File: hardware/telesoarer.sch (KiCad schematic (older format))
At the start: 30 parts, among them IC1 ATMEGA328P, K1 RC SIG IN, K2 G T R, P1 ATMEL ISP, P2 PZ, P3 PZ_IN, P4 AOUT, Q1 BC847C, Q2 2N7000, U1 MS5611

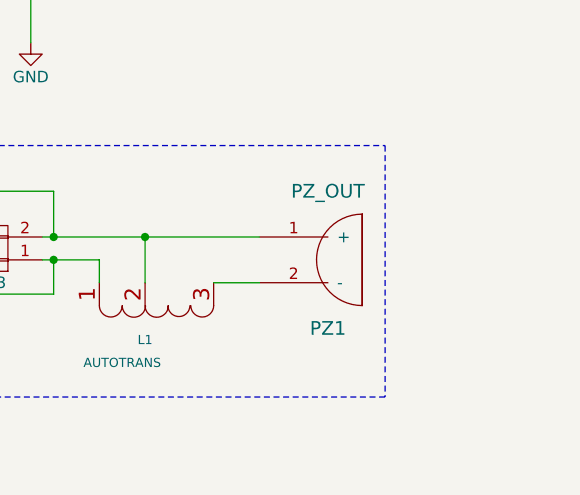
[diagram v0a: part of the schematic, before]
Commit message: Moved high voltage piezo output away from delicate analog output. Other minor changes.
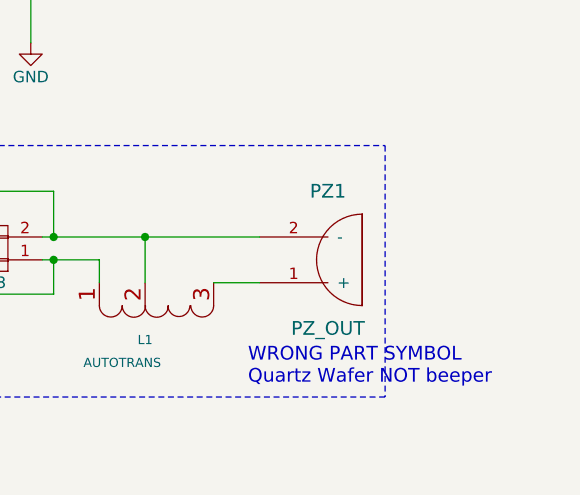
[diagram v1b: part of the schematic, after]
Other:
- note added: "WRONG PART SYMBOL\nQuartz Wafer NOT beeper"
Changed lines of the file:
@@
 F 3 "" H 9500 5450 60  0001 C CNN
 	1    9500 5450
-	1    0    0    -1
+	1    0    0    1
 $EndComp
 $Comp
@@
 Connection ~ 8400 5450
 Connection ~ 7200 5600
+Text Notes 9250 6000 0    60   ~ 0
+WRONG PART SYMBOL\nQuartz Wafer NOT beeper
 $EndSCHEMATC

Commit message: Need 16MHz xtal for Arduino bootloader serial to work -- clock too inaccurate at 8MHz RC. Added OLED display and the somewhat important 3.3V regulator I completely forgot about before!
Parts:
- removed K2: G T R, footprints:TP-3, symbol CONN_01X03
- added C10, C11, C12, C13: 1u, footprints:C_0603, symbol C-RESCUE-telesoarer-mlf
- added C14, C15: 2u2, footprints:C_0603, symbol C-RESCUE-telesoarer-mlf
- added C5, C6: 18p, footprints:C_0603, symbol C-RESCUE-telesoarer-mlf
- added C7, C9: 0u1, footprints:C_0603, symbol C-RESCUE-telesoarer-mlf
- added C8: 22u, footprints:TantalC_SizeS_EIA-3216, symbol CP
- added P5: OLED 0.91\" 128x32, symbol CONN_01X15
- added R12: 1K, footprints:R_0603, symbol R
- added R13: 0, footprints:R_0603, symbol R
- added R14: 390K, footprints:R_0603, symbol R
- added U2: LM1117IMP-3.3/NOPB, TO_SOT_Packages_SMD:SOT-223, symbol AP111733
- added X1: 16MHz, symbol CRYSTAL_SMD
- K1: value RC SIG IN -> DATA; symbol CONN_01X03 -> CONN_01X06
- R1: value 5K6 -> 10K
- R2: value 200 -> 1K
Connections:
- net labels added: +BATT, D/~C, OLED_~SS, RX, SENS_~SS, TX, VBAT, VDD, VSS, ~RES, ~RESET
- net labels removed: +5V, RESET, ~SS
- wire segments 96 -> 147
- no-connect marks 13 -> 8
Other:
- note added: "All ATmega328 I/O pins have clamping diodes and \ntherefore should be fine sinking 5V, so long as a \nseries current limiting resistor is present."
- note added: "MCU 5 Volt SIG & RX inputs with 3.3V VDD"
- note added: "WRONG SYMBOL\nQuartz Wafer\nNOT beeper"
- note removed: "Debug UART\nBreak-out"
- note removed: "WRONG PART SYMBOL\nQuartz Wafer NOT beeper"
- moved on the sheet: C1, C2, C3, C4, D1, D2, D3, P4, Q2, R1, R10, R11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

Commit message: Switching to NXP ARM chip. Added reference files.
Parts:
- removed C2: 22u, footprints:TantalC_SizeS_EIA-3216, symbol CP
- removed U2: LM1117IMP-3.3/NOPB, TO_SOT_Packages_SMD:SOT-223, symbol AP111733
- added U2: MCP1703T-3302, footprints:SOT-23A, symbol MCP1703T-3302
- C1: renamed from C4; footprint footprints:C_0603 -> footprints:C_0402
- C10: renamed from C11; footprint footprints:C_0603 -> footprints:C_0402
- C11: renamed from C12; footprint footprints:C_0603 -> footprints:C_0402
- C12: renamed from C13; footprint footprints:C_0603 -> footprints:C_0402
- C13: renamed from C14; footprint footprints:C_0603 -> footprints:C_0402
- C14: renamed from C15; footprint footprints:C_0603 -> footprints:C_0402
- C2: renamed from C7; footprint footprints:C_0603 -> footprints:C_0402
- C4: renamed from C5; footprint footprints:C_0603 -> footprints:C_0402
- C5: renamed from C9; footprint footprints:C_0603 -> footprints:C_0402
- C6: footprint footprints:C_0603 -> footprints:C_0402
- C7: renamed from C1; footprint footprints:C_0603 -> footprints:C_0402
- C8: renamed from C3; footprint footprints:C_0603 -> footprints:C_0402
- C9: renamed from C10; footprint footprints:C_0603 -> footprints:C_0402
- K1: footprint footprints:SIL-3 -> Pin_Headers:Pin_Header_Angled_1x06
- P5: footprint (none) -> footprints:ZIF_FPC15
- R1, R14, R2, R3, R4, R5: footprint footprints:R_0603 -> footprints:R_0402
- R10: renamed from R8; footprint footprints:R_0603 -> footprints:R_0402
- R11: renamed from R9; footprint footprints:R_0603 -> footprints:R_0402
- R12: renamed from R10; footprint footprints:R_0603 -> footprints:R_0402
- R13: renamed from R11; footprint footprints:R_0603 -> footprints:R_0402
- R6: renamed from R12; footprint footprints:R_0603 -> footprints:R_0402
- R7: renamed from R13; footprint footprints:R_0603 -> footprints:R_0402
- R8: renamed from R7; footprint footprints:R_0603 -> footprints:R_0402
- R9: renamed from R6; footprint footprints:R_0603 -> footprints:R_0402
- X1: footprint (none) -> Crystals:Crystal_SMD_2520_4Pads
- renumbered C8 to C3
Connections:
- wire segments 147 -> 139
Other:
- moved on the sheet: C1, C7

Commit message: Ripping things apart for the change to STM32 chipa
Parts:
- removed C2: 0u1, footprints:C_0402, symbol C-RESCUE-telesoarer-mlf
- removed IC1: ATMEGA328P, footprints:MLF-32_2mmVIA_SINK, symbol ATMEGA328P
- removed P1: ATMEL ISP, footprints:PIN_ARRAY_3x2_GRUVIN, symbol CONN_01X06
- removed R1: 10K, footprints:R_0402, symbol R
- removed R6: 1K, footprints:R_0402, symbol R
- removed R7: 0, footprints:R_0402, symbol R
- added C7, C8, C9: 0u1, footprints:C_0402, symbol C-RESCUE-telesoarer-mlf
- added IC1: STM32F103TBU6, footprints:VFQFPN36_0.5_6x6, symbol STM32F103TBU6
- added K2: SERIAL, Pin_Headers:Pin_Header_Angled_1x03, symbol CONN_01X03
- added K3: DEBUG, Pin_Headers:Pin_Header_Angled_1x03, symbol CONN_01X03
- added R2: NC, footprints:R_0603, symbol R
- added R3: 5K, footprints:R_0402, symbol R
- K1: value DATA -> RC_SIG; footprint Pin_Headers:Pin_Header_Angled_1x06 -> Pin_Headers:Pin_Header_Angled_1x03; symbol CONN_01X06 -> CONN_01X03
- renumbered C8 to C10, C9 to C11, C10 to C12, C11 to C13, C12 to C14, C13 to C15, C14 to C16, C4 to C2, C6 to C4, C7 to C6, P2 to P1, P3 to P2, P4 to P3, P5 to P4, R2 to R1, R11 to R10, R12 to R11, R13 to R12, R14 to R13, R3 to R4, R4 to R5, R5 to R6, R9 to R7, R10 to R9
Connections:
- net labels added: OLED_D/~C, OLED_~RES, SWDCLK, SWDIO, USART1_RX, USART1_TX, USRAT1_RX
- net labels removed: D/~C, RX, TX, ~RES
- wire segments 139 -> 152
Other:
- note removed: "3x2 pogo\npin pads"
- moved on the sheet: C1, C10, C13, C14, C2, C3, C4, C5, C6, D1, D2, D3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

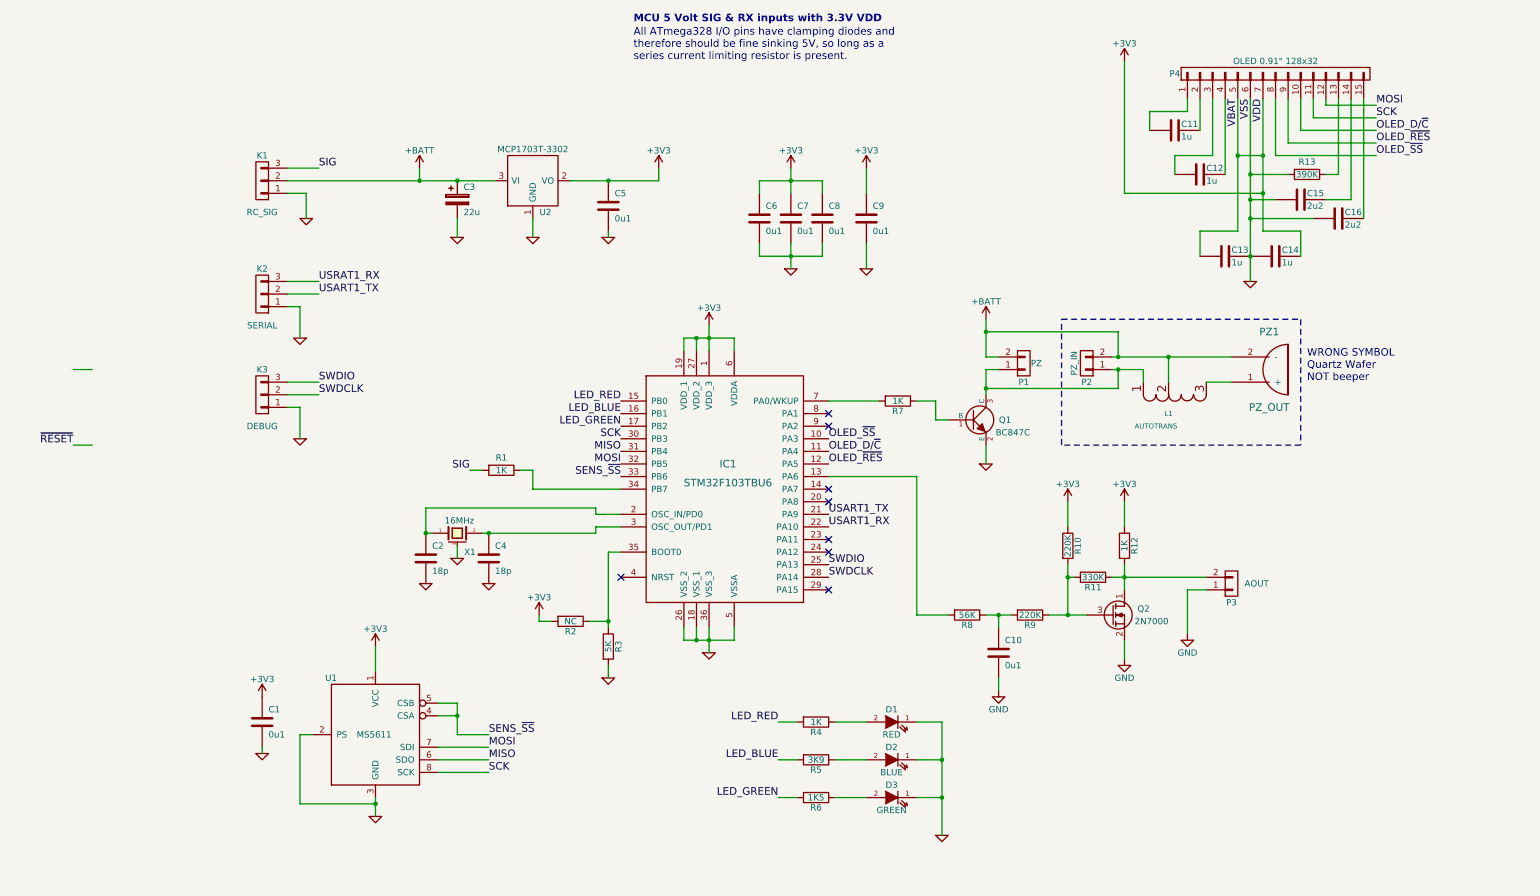
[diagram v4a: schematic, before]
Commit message: Schematic updates for change to STM32F103 MCU
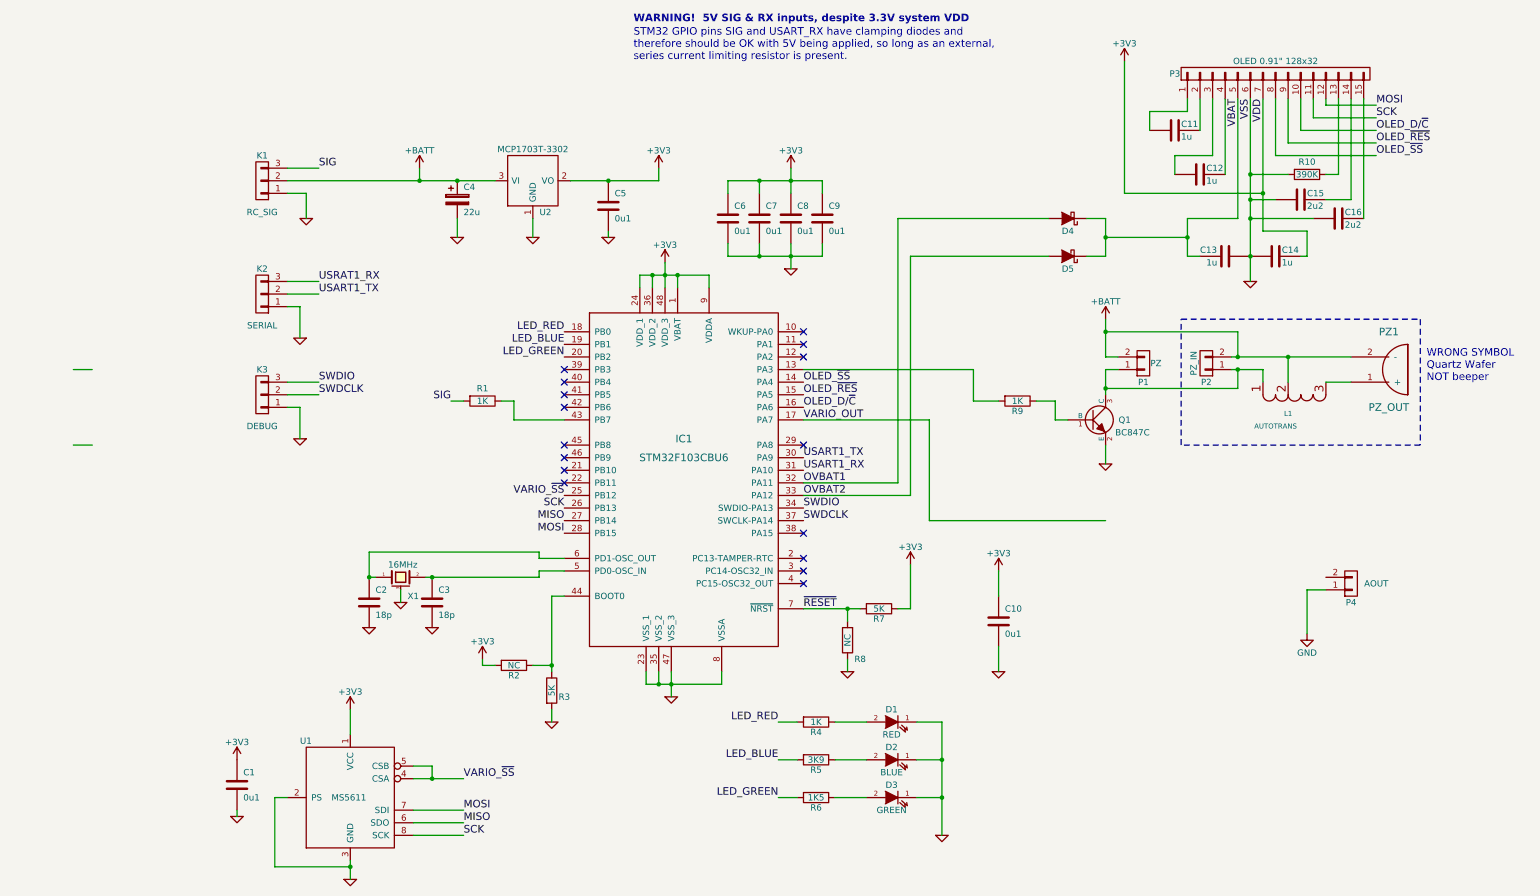
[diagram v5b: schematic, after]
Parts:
- removed C10: 0u1, footprints:C_0402, symbol C-RESCUE-telesoarer-mlf
- removed IC1: STM32F103TBU6, footprints:VFQFPN36_0.5_6x6, symbol STM32F103TBU6
- removed Q2: 2N7000, TO_SOT_Packages_SMD:SOT-23, symbol Q_NMOS_DSG
- removed R10, R9: 220K, footprints:R_0402, symbol R
- removed R11: 330K, footprints:R_0402, symbol R
- removed R12: 1K, footprints:R_0402, symbol R
- added C6: 0u1, footprints:C_0402, symbol C-RESCUE-telesoarer-mlf
- added D4, D5: D_Schottky, symbol D_Schottky
- added IC1: STM32F103CBU6, symbol STM32F103CBU6
- added R7: 5K, footprints:R_0402, symbol R
- R8: value 56K -> NC
- renumbered C9 to C10, C4 to C3, C3 to C4, C6 to C7, C7 to C8, C8 to C9, P4 to P3, P3 to P4, R13 to R10, R7 to R9
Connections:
- net +3V3: now also C6.1, IC1.1 (VBAT), IC1.24 (VDD_1), IC1.36 (VDD_2), IC1.48 (VDD_3), IC1.9 (VDDA), R7.1; no longer C13.2, P3.5 (P5)
- net GND: now also R8.1, C6.2, IC1.23 (VSS_1), IC1.35 (VSS_2), IC1.47 (VSS_3), IC1.8 (VSSA)
- net LED_BLUE: now also IC1.19 (PB1)
- net LED_GREEN: now also IC1.20 (PB2)
- net LED_RED: now also IC1.18 (PB0)
- net MISO: now also IC1.27 (PB14)
- net MOSI: now also IC1.28 (PB15)
- net OLED_D/~C: now also IC1.16 (PA6)
- net OLED_~RES: now also IC1.15 (PA5)
- net OLED_~SS: now also IC1.14 (PA4)
- net SCK: now also IC1.26 (PB13)
- net SWDCLK: now also IC1.37 (SWCLK-PA14)
- net SWDIO: now also IC1.34 (SWDIO-PA13)
- net USART1_RX: now also IC1.31 (PA10)
- net USART1_TX: now also IC1.30 (PA9)
- net ~RESET: now also R8.2, IC1.7 (~NRST), R7.2
- net at R9.2: now also IC1.13 (PA3)
- net at R1.1: now also IC1.43 (PB7)
- net at C2.1, X1.1: now also IC1.6 (PD1-OSC_OUT)
- net at C3.1, X1.2: now also IC1.5 (PD0-OSC_IN)
- net at R2.1, R3.1: now also IC1.44 (BOOT0)
- net SENS_~SS renamed VARIO_~SS
- net VARIO_~SS: now also IC1.25 (PB12)
- new net OVBAT1: D4.2 (A), IC1.32 (PA11)
- new net OVBAT2: D5.2 (A), IC1.33 (PA12)
- new net VARIO_OUT: IC1.17 (PA7)
- new net VBAT: C13.2, D4.1 (K), D5.1 (K), P3.5 (P5)
- no-connect marks 8 -> 16
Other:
- note added: "STM32 GPIO pins SIG and USART_RX have clamping diodes and \ntherefore should be OK with 5V being applied, so long as an external,\nseries current limiting resistor is present."
- note added: "WARNING! 5V SIG & RX inputs, despite 3.3V system VDD"
- note removed: "All ATmega328 I/O pins have clamping diodes and \ntherefore should be fine sinking 5V, so long as a \nseries current limiting resistor is present."
- note removed: "MCU 5 Volt SIG & RX inputs with 3.3V VDD"
- moved on the sheet: C1, C10, C2, C3, L1, P1, P2, P4, PZ1, Q1, R1, R2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

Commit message: Completed first draft of STM32 based schematic. (Added Vario output LPF.)
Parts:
- added C11, C14: 0u1, footprints:C_0402, symbol C-RESCUE-telesoarer-mlf
- added R10, R11: 5K, footprints:R_0402, symbol R
- added R12, R15: 100K, footprints:R_0402, symbol R
- added R13: 100, footprints:R_0402, symbol R
- added U3: AD8027ARTZ, symbol AD8027ARTZ
- C2, C3: symbol C-RESCUE-telesoarer-mlf -> C
- renumbered C11 to C12, C12 to C13, C13 to C15, C14 to C16, C15 to C17, C16 to C18, R10 to R14, R8 to R7, R7 to R8
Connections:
- net USRAT1_RX is gone; now on net USART1_RX: K2.3 (P3)
- net +3V3: now also U3.6 (V+)
- net GND: now also C11.2, C14.2, R13.1, U3.2 (V-)
- net VARIO_OUT: now also R10.2
- net at P4.2 (P2): now also R15.2, U3.1
- new net: R12.2, U3.3 (+)
- new net: R13.2, R15.1, U3.4 (-)
- new net: C14.1, R11.1, R12.1
- new net: C11.1, R10.1, R11.2
- no-connect marks 16 -> 17
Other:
- moved on the sheet: C1, C10, C4, C5, K1, P4, R9, U1, U2

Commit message: Work on STM32 / OLED PCB design begins
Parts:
- removed K2: SERIAL, Pin_Headers:Pin_Header_Angled_1x03, symbol CONN_01X03
- removed K3: DEBUG, Pin_Headers:Pin_Header_Angled_1x03, symbol CONN_01X03
- added P5: CONN_01X05, Connectors_JST:JST_SH_SM05B-SRSS-TB_05x1.00mm_Angled, symbol CONN_01X05
- D4, D5: footprint (none) -> Diodes_SMD:SOD-523
- IC1: value STM32F103CBU6 -> STM32F103CBT6; footprint (none) -> footprints:LQFP-48_7x7mm_Pitch0.5mm; symbol STM32F103CBU6 -> STM32F103CBT6
- P1, P2: footprint footprints:PIN_ARRAY_2X1 -> Connectors_JST:JST_SH_SM02B-SRSS-TB_02x1.00mm_Angled
- U3: footprint (none) -> TO_SOT_Packages_SMD:SOT-23-6
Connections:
- net GND: now also P5.1 (P1)
- net SWDCLK: now also P5.2 (P2)
- net SWDIO: now also P5.3 (P3)
- net USART1_RX: now also P5.5 (P5)
- net USART1_TX: now also P5.4 (P4)
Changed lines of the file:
@@
 F 0 "P1" H 8050 3750 50  0000 C CNN
 F 1 "PZ" H 8150 3600 50  0000 C CNN
-F 2 "footprints:PIN_ARRAY_2X1" H 8050 3600 50  0001 C CNN
+F 2 "Connectors_JST:JST_SH_SM02B-SRSS-TB_02x1.00mm_Angled" H 8050 3600 50  0001 C CNN
 F 3 "" H 8050 3600 50  0000 C CNN
 	1    8050 3600
@@
 F 0 "P2" H 8550 3750 50  0000 C CNN
 F 1 "PZ_IN" V 8650 3600 50  0000 C CNN
-F 2 "footprints:PIN_ARRAY_2X1" H 8550 3600 50  0001 C CNN
+F 2 "Connectors_JST:JST_SH_SM02B-SRSS-TB_02x1.00mm_Angled" H 8550 3600 50  0001 C CNN
 F 3 "" H 8550 3600 50  0000 C CNN
 	1    8550 3600
@@
 	1150 7400 1750 7400
 Connection ~ 1750 7400
-Wire Wire Line
-	-450 4250 -300 4250
 Text Label 3450 4650 2    60   ~ 0
 VARIO_~SS
@@
 Wire Wire Line
 	1900 5100 1900 5350
-Wire Wire Line
-	-300 3650 -450 3650
 Text Label 5350 3750 0    60   ~ 0
 OLED_~SS
@@
 Text Label 5350 4450 0    60   ~ 0
 USART1_RX
-$Comp
-L CONN_01X03 K2
-U 1 1 5822DCA2
-P 1050 3050
-F 0 "K2" H 1050 2850 50  0000 C CNN
-F 1 "SERIAL" H 1050 3300 50  0000 C CNN
-F 2 "Pin_Headers:Pin_Header_Angled_1x03" H 1000 3400 50  0001 C CNN
-F 3 "" H 1050 3050 50  0000 C CNN
-	1    1050 3050
-	-1   0    0    1
-$EndComp
-$Comp
-L GND #PWR028
-U 1 1 5822DD54
-P 1350 3400
-F 0 "#PWR028" H 1350 3400 30  0001 C CNN
-F 1 "GND" H 1350 3330 30  0001 C CNN
-F 2 "" H 1350 3400 60  0001 C CNN
-F 3 "" H 1350 3400 60  0001 C CNN
-	1    1350 3400
-	-1   0    0    -1
-$EndComp
-Wire Wire Line
-	1350 3400 1350 3150
 Wire Wire Line
-	1350 3150 1250 3150
+	1250 3150 1500 3150
 Wire Wire Line
-	1250 3750 1500 3750
-Wire Wire Line
-	1250 3850 1500 3850
-Text Label 1500 3750 0    60   ~ 0
+	1250 3250 1500 3250
+Text Label 1500 3150 0    60   ~ 0
 SWDIO
-Text Label 1500 3850 0    60   ~ 0
+Text Label 1500 3250 0    60   ~ 0
 SWDCLK
 $Comp
-L CONN_01X03 K3
-U 1 1 5822DEEB
-P 1050 3850
-F 0 "K3" H 1050 3650 50  0000 C CNN
-F 1 "DEBUG" H 1050 4100 50  0000 C CNN
-F 2 "Pin_Headers:Pin_Header_Angled_1x03" H 1000 4200 50  0001 C CNN
-F 3 "" H 1050 3850 50  0000 C CNN
-	1    1050 3850
-	-1   0    0    1
-$EndComp
-$Comp
-L GND #PWR029
+L GND #PWR028
 U 1 1 5822DEF1
-P 1350 4200
-F 0 "#PWR029" H 1350 4200 30  0001 C CNN
-F 1 "GND" H 1350 4130 30  0001 C CNN
-F 2 "" H 1350 4200 60  0001 C CNN
-F 3 "" H 1350 4200 60  0001 C CNN
-	1    1350 4200
+P 1350 3600
+F 0 "#PWR028" H 1350 3600 30  0001 C CNN
+F 1 "GND" H 1350 3530 30  0001 C CNN
+F 2 "" H 1350 3600 60  0001 C CNN
+F 3 "" H 1350 3600 60  0001 C CNN
+	1    1350 3600
 	-1   0    0    -1
 $EndComp
 Wire Wire Line
-	1350 4200 1350 3950
+	1350 3600 1350 3350
 Wire Wire Line
-	1350 3950 1250 3950
+	1350 3350 1250 3350
 Wire Wire Line
 	3050 4050 3450 4050
@@
 	7350 4050 7450 4050
 $Comp
-L STM32F103CBU6 IC1
+L STM32F103CBT6 IC1
 U 1 1 58364B57
 P 4400 4500
 F 0 "IC1" H 4400 4800 60  0000 C CNN
-F 1 "STM32F103CBU6" H 4400 4650 60  0000 C CNN
-F 2 "" H 4350 4850 60  0001 C CNN
+F 1 "STM32F103CBT6" H 4400 4650 60  0000 C CNN
+F 2 "footprints:LQFP-48_7x7mm_Pitch0.5mm" H 4350 4850 60  0001 C CNN
 F 3 "" H 4350 4850 60  0001 C CNN
 	1    4400 4500
@@
 F 0 "D4" H 7450 2550 50  0000 C CNN
 F 1 "D_Schottky" H 7450 2350 50  0001 C CNN
-F 2 "" H 7450 2450 50  0000 C CNN
+F 2 "Diodes_SMD:SOD-523" H 7450 2450 50  0001 C CNN
 F 3 "" H 7450 2450 50  0000 C CNN
 	1    7450 2450
@@
 F 0 "D5" H 7450 2850 50  0000 C CNN
 F 1 "D_Schottky" H 7450 2950 50  0001 C CNN
-F 2 "" H 7450 2750 50  0000 C CNN
+F 2 "Diodes_SMD:SOD-523" H 7450 2750 50  0001 C CNN
 F 3 "" H 7450 2750 50  0000 C CNN
 	1    7450 2750
@@
 $EndComp
 $Comp
-L +3V3 #PWR030
+L +3V3 #PWR029
 U 1 1 5836ADAE
 P 6200 5200
-F 0 "#PWR030" H 6200 5050 50  0001 C CNN
+F 0 "#PWR029" H 6200 5050 50  0001 C CNN
 F 1 "+3V3" H 6200 5340 50  0000 C CNN
 F 2 "" H 6200 5200 50  0000 C CNN
@@
 $EndComp
 $Comp
-L GND #PWR031
+L GND #PWR030
 U 1 1 5836AFEF
 P 5700 6050
-F 0 "#PWR031" H 5700 6050 30  0001 C CNN
+F 0 "#PWR030" H 5700 6050 30  0001 C CNN
 F 1 "GND" H 5700 5980 30  0001 C CNN
 F 2 "" H 5700 6050 60  0001 C CNN
@@
 F 0 "U3" H 9600 4900 50  0000 L CNN
 F 1 "AD8027ARTZ" H 9650 5200 50  0000 L CNN
-F 2 "" H 9450 5100 50  0000 C CNN
+F 2 "TO_SOT_Packages_SMD:SOT-23-6" H 9450 5100 50  0001 C CNN
 F 3 "" H 9550 5200 50  0000 C CNN
 	1    9550 5050
@@
 Connection ~ 8050 4950
 $Comp
-L GND #PWR032
+L GND #PWR031
 U 1 1 5836D42B
 P 8550 5600
-F 0 "#PWR032" H 8550 5350 50  0001 C CNN
+F 0 "#PWR031" H 8550 5350 50  0001 C CNN
 F 1 "GND" H 8550 5450 50  0000 C CNN
 F 2 "" H 8550 5600 50  0000 C CNN
@@
 $EndComp
 $Comp
-L GND #PWR033
+L GND #PWR032
 U 1 1 5836D4D5
 P 8050 5600
-F 0 "#PWR033" H 8050 5350 50  0001 C CNN
+F 0 "#PWR032" H 8050 5350 50  0001 C CNN
 F 1 "GND" H 8050 5450 50  0000 C CNN
 F 2 "" H 8050 5600 50  0000 C CNN
@@
 	8550 5600 8550 5500
 $Comp
-L GND #PWR034
+L GND #PWR033
 U 1 1 5836D79A
 P 9150 5950
-F 0 "#PWR034" H 9150 5700 50  0001 C CNN
+F 0 "#PWR033" H 9150 5700 50  0001 C CNN
 F 1 "GND" H 9150 5800 50  0000 C CNN
 F 2 "" H 9150 5950 50  0000 C CNN
@@
 	9450 5350 9450 5400
 $Comp
-L GND #PWR035
+L GND #PWR034
 U 1 1 5836DA64
 P 9450 5400
-F 0 "#PWR035" H 9450 5150 50  0001 C CNN
+F 0 "#PWR034" H 9450 5150 50  0001 C CNN
 F 1 "GND" H 9450 5250 50  0000 C CNN
 F 2 "" H 9450 5400 50  0000 C CNN
@@
 $EndComp
 $Comp
-L +3V3 #PWR036
+L +3V3 #PWR035
 U 1 1 5836DB0E
 P 9450 4700
-F 0 "#PWR036" H 9450 4550 50  0001 C CNN
+F 0 "#PWR035" H 9450 4550 50  0001 C CNN
 F 1 "+3V3" H 9450 4840 50  0000 C CNN
 F 2 "" H 9450 4700 50  0000 C CNN
@@
 Wire Wire Line
 	1500 2950 1250 2950
+$Comp
+L CONN_01X05 P5
+U 1 1 5837D856
+P 1050 3150
+F 0 "P5" H 1050 3450 50  0000 C CNN
+F 1 "CONN_01X05" V 1150 3150 50  0000 C CNN
+F 2 "Connectors_JST:JST_SH_SM05B-SRSS-TB_05x1.00mm_Angled" H 1050 3150 50  0001 C CNN
+F 3 "" H 1050 3150 50  0000 C CNN
+	1    1050 3150
+	-1   0    0    1
+$EndComp
 $EndSCHEMATC
